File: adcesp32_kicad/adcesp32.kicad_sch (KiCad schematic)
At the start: 16 parts, among them IC1 PCM1862DBT, J1 AudioJack4, J2 USB_C_Receptacle_USB2.0_16P, J3 RCJ-2112, SW1 SW_Push, SW2 SW_Push, U1 ESP32-S3-WROOM-1, U2 AMS1117-3.3

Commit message: updated schematic
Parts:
- added C10, C11, C4, C5, C6, C7, C8, C9: C, symbol Device:C
- added D1, D2: LED, symbol Device:LED
- added J4, J5: Conn_01x05_Pin, symbol Connector:Conn_01x05_Pin
- added J6, J7: Conn_01x04_Pin, symbol Connector:Conn_01x04_Pin
- added L1: L_Small, symbol Device:L_Small
- added R6, R7: R, symbol Device:R
- IC1: footprint SOP50P640X120-30N -> KiCad:SOP50P640X120-30N
- J3: footprint RCJ2112 -> KiCad:RCJ2112
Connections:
- net +3V3: now also IC1.13 (DVDD), IC1.14 (IOVDD), C10.2, C11.2, C6.2, C7.2, J7.2 (Pin_2), L1.1, R7.2
- net BCK: now also J4.4 (Pin_4)
- net DOUT_ADC: now also J4.2 (Pin_2)
- net GND: now also IC1.12 (DGND), IC1.7 (AGND), C10.1, C11.1, C6.1, C7.1, C8.1, C9.1, D1.1 (K), D2.1 (K), J7.1 (Pin_1)
- net I2S_DOUT: now also J4.1 (Pin_1)
- net L1: now also C5.1; no longer IC1.3 (VINL1/VIN1P)
- net LRCK: now also J4.3 (Pin_3)
- net R1: now also C4.1; no longer IC1.4 (VINR1/VIN2P)
- net SCL: now also J7.3 (Pin_3)
- net SDA: now also J7.4 (Pin_4)
- net ESP_GPIO17: now reaches U1.10 (IO17)
- net ESP_GPIO17: now also J5.2 (Pin_2)
- net ESP_GPIO18: now reaches U1.11 (IO18)
- net ESP_GPIO18: now also J5.3 (Pin_3)
- net ESP_GPIO38: now reaches U1.31 (IO38)
- net ESP_GPIO38: now also J5.1 (Pin_1)
- net ESP_GPIO2: now reaches U1.38 (IO2)
- net ESP_GPIO2: now also J5.4 (Pin_4)
- net ESP_GPIO1: now reaches U1.39 (IO1)
- net ESP_GPIO1: now also J5.5 (Pin_5)
- net at U1.4 (IO4): now also R6.2
- net at IC1.11 (LDO): now also C9.2
- net SCKI: now reaches IC1.15 (SCKI)
- net SCKI: now also J4.5 (Pin_5)
- net ADC_GPIO3: now reaches IC1.19 (INT)
- net ADC_GPIO3: now also J6.4 (Pin_4)
- net ADC_GPIO2: now reaches IC1.20 (MD6)
- net ADC_GPIO2: now also J6.3 (Pin_3)
- net ADC_GPIO1: now reaches IC1.21 (MD5)
- net ADC_GPIO1: now also J6.2 (Pin_2)
- net ADC_GPIO0: now reaches IC1.22 (MD4)
- net ADC_GPIO0: now also J6.1 (Pin_1)
- net at IC1.6 (VREF): now also C8.2
- net AVDD: now reaches IC1.8 (AVDD)
- net AVDD: now also L1.2
- new net: C4.2, IC1.4 (VINR1/VIN2P)
- new net: C5.2, IC1.3 (VINL1/VIN1P)
- new net: D1.2 (A), R7.1
- new net: D2.2 (A), R6.1
- no-connect marks 3 -> 33
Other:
- moved on the sheet: C3, IC1, J1, J3, R2, R3, U1

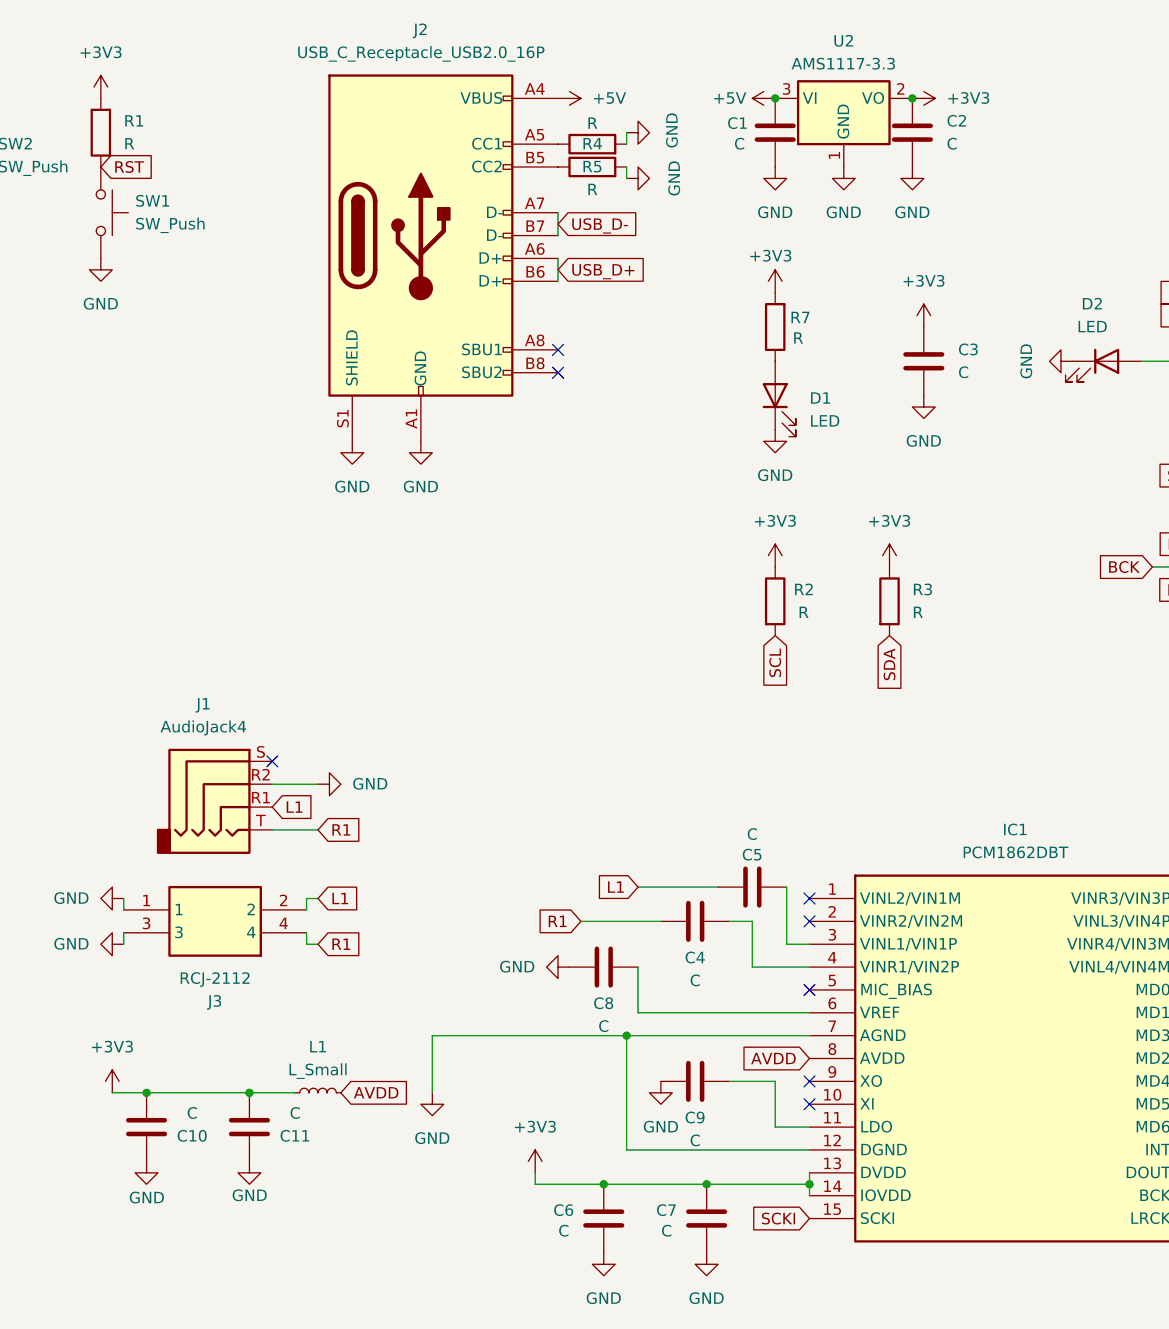
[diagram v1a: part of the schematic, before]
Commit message: added cap values
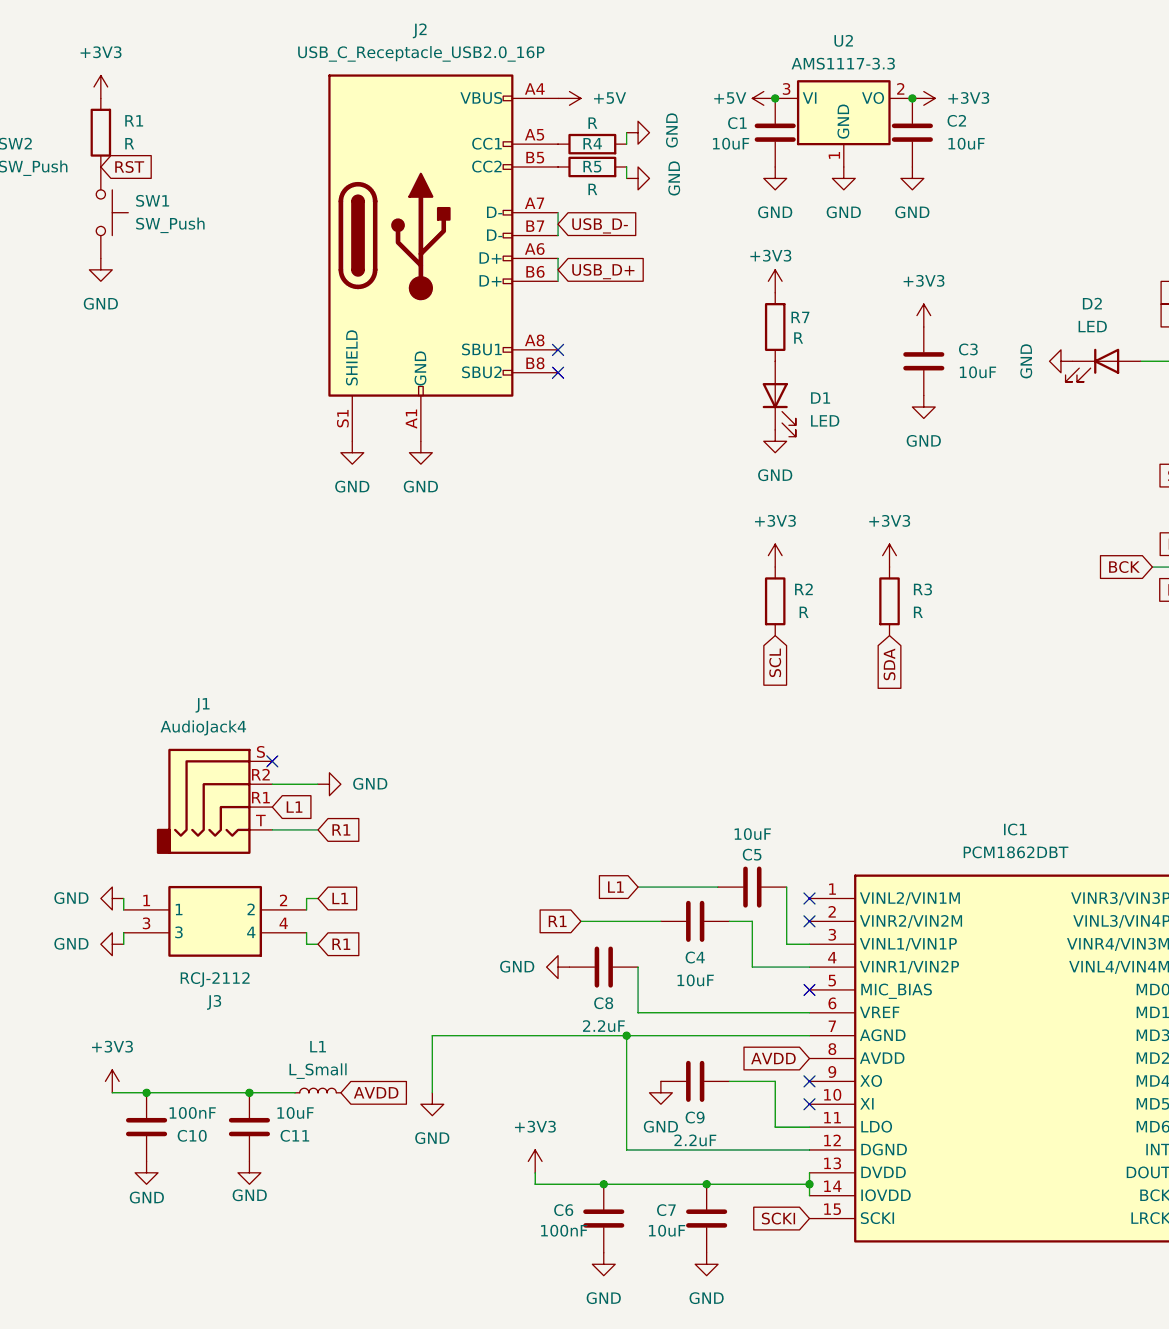
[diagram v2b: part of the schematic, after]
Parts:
- C1, C11, C2, C3, C4, C5, C7: value C -> 10uF; footprint (none) -> Capacitor_SMD:C_0402_1005Metric
- C10, C6: value C -> 100nF; footprint (none) -> Capacitor_SMD:C_0402_1005Metric
- C8, C9: value C -> 2.2uF; footprint (none) -> Capacitor_SMD:C_0402_1005Metric
- J4, J5: footprint (none) -> Connector_PinHeader_1.00mm:PinHeader_1x05_P1.00mm_Vertical
- J6, J7: footprint (none) -> Connector_PinHeader_1.00mm:PinHeader_1x04_P1.00mm_Vertical
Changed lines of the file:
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@@
 			)
 		)
-		(property "Footprint" ""
+		(property "Footprint" "Connector_PinHeader_1.00mm:PinHeader_1x04_P1.00mm_Vertical"
 			(at 248.92 146.05 0)
 			(effects
@@
 			)
 		)
-		(property "Value" "C"
+		(property "Value" "10uF"
 			(at 107.95 122.174 90)
 			(effects
@@
 			)
 		)
-		(property "Footprint" ""
+		(property "Footprint" "Capacitor_SMD:C_0402_1005Metric"
 			(at 111.76 114.6048 0)
 			(effects
@@
 			)
 		)
-		(property "Value" "C"
+		(property "Value" "10uF"
 			(at 135.89 29.2099 0)
 			(effects
@@
 			)
 		)
-		(property "Footprint" ""
+		(property "Footprint" "Capacitor_SMD:C_0402_1005Metric"
 			(at 133.0452 31.75 0)
 			(effects
@@
 			)
 		)
-		(property "Footprint" ""
+		(property "Footprint" "Connector_PinHeader_1.00mm:PinHeader_1x05_P1.00mm_Vertical"
 			(at 246.38 111.76 0)
 			(effects
@@
 			)
 		)
-		(property "Footprint" ""
+		(property "Footprint" "Connector_PinHeader_1.00mm:PinHeader_1x04_P1.00mm_Vertical"
 			(at 248.92 129.54 0)
 			(effects
@@
 			)
 		)
-		(property "Value" "C"
+		(property "Value" "10uF"
 			(at 114.3 105.918 90)
 			(effects
@@
 			)
 		)
-		(property "Footprint" ""
+		(property "Footprint" "Capacitor_SMD:C_0402_1005Metric"
 			(at 118.11 110.7948 0)
 			(effects
@@
 			)
 		)
-		(property "Value" "C"
+		(property "Value" "10uF"
 			(at 137.16 54.6099 0)
 			(effects
@@
 			)
 		)
-		(property "Footprint" ""
+		(property "Footprint" "Capacitor_SMD:C_0402_1005Metric"
 			(at 134.3152 57.15 0)
 			(effects
@@
 			)
 		)
-		(property "Value" "C"
+		(property "Value" "100nF"
 			(at 93.345 149.987 0)
 			(effects
@@
 			)
 		)
-		(property "Footprint" ""
+		(property "Footprint" "Capacitor_SMD:C_0402_1005Metric"
 			(at 96.8248 144.78 0)
 			(effects
@@
 			)
 		)
-		(property "Value" "C"
+		(property "Value" "10uF"
 			(at 104.775 149.987 0)
 			(effects
@@
 			)
 		)
-		(property "Footprint" ""
+		(property "Footprint" "Capacitor_SMD:C_0402_1005Metric"
 			(at 108.2548 144.78 0)
 			(effects
@@
 			)
 		)
-		(property "Value" "C"
+		(property "Value" "2.2uF"
 			(at 107.95 139.954 90)
 			(effects
@@
 			)
 		)
-		(property "Footprint" ""
+		(property "Footprint" "Capacitor_SMD:C_0402_1005Metric"
 			(at 111.76 132.3848 0)
 			(effects
@@
 			)
 		)
-		(property "Value" "C"
-			(at 112.268 29.21 0)
+		(property "Value" "10uF"
+			(at 109.728 29.21 0)
 			(effects
 				(font
@@
 			)
 		)
-		(property "Footprint" ""
+		(property "Footprint" "Capacitor_SMD:C_0402_1005Metric"
 			(at 117.8052 31.75 0)
 			(effects
@@
 			)
 		)
-		(property "Value" "C"
+		(property "Value" "2.2uF"
 			(at 97.79 127.254 90)
 			(effects
@@
 			)
 		)
-		(property "Footprint" ""
+		(property "Footprint" "Capacitor_SMD:C_0402_1005Metric"
 			(at 101.6 119.6848 0)
 			(effects
@@
 			)
 		)
-		(property "Footprint" ""
+		(property "Footprint" "Connector_PinHeader_1.00mm:PinHeader_1x05_P1.00mm_Vertical"
 			(at 246.38 92.71 0)
 			(effects
@@
 			)
 		)
-		(property "Value" "C"
+		(property "Value" "10uF"
 			(at 63.5 136.906 0)
 			(effects
@@
 			)
 		)
-		(property "Footprint" ""
+		(property "Footprint" "Capacitor_SMD:C_0402_1005Metric"
 			(at 57.4548 134.62 0)
 			(effects
@@
 			)
 		)
-		(property "Value" "C"
+		(property "Value" "100nF"
 			(at 52.07 136.906 0)
 			(effects
@@
 			)
 		)
-		(property "Footprint" ""
+		(property "Footprint" "Capacitor_SMD:C_0402_1005Metric"
 			(at 46.0248 134.62 0)
 			(effects

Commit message: completed pcb design
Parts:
- removed J1: AudioJack4, symbol Connector_Audio:AudioJack4
- removed SW1, SW2: SW_Push, symbol Switch:SW_Push
- added C12: 10uF, Capacitor_SMD:C_0402_1005Metric, symbol Device:C
- added J8: Conn_01x04_Pin, Connector_PinHeader_1.00mm:PinHeader_1x04_P1.00mm_Vertical, symbol Connector:Conn_01x04_Pin
- added J9: SJ-43514, SJ43514, symbol SJ-43514:SJ-43514
- added R8: 0.5Ohm, Resistor_SMD:R_0603_1608Metric, symbol Device:R
- added R9: 10kOhm, Resistor_SMD:R_0402_1005Metric, symbol Device:R
- added S1, S2, S3: TS-1187, KiCad:SW_TS-1187A-B-A-B, symbol TS-1187A-B-A-B:TS-1187A-B-A-B
- D1, D2: footprint (none) -> Resistor_SMD:R_0805_2012Metric
- J2: footprint (none) -> Connector_USB:USB_C_Receptacle_HRO_TYPE-C-31-M-12
- L1: value L_Small -> 10uH; footprint (none) -> Inductor_SMD:L_0805_2012Metric
- R1: value R -> 10kOhm; footprint (none) -> Resistor_SMD:R_0402_1005Metric
- R2, R3, R6, R7: value R -> 2.2kOhm; footprint (none) -> Resistor_SMD:R_0603_1608Metric
- R4, R5: value R -> 5.1kOhm; footprint (none) -> Resistor_SMD:R_0402_1005Metric
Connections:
- net +3V3: now also J8.4 (Pin_4), R8.2, R9.2; no longer C2.1
- net BOOT: now also S1.C, S1.D
- net GND: now also C12.1, J8.3 (Pin_3), J9.4 (RING_2), S1.A, S1.B, S2.A, S2.B, S3.A, S3.B
- net L1: now also J9.3 (RING_1)
- net R1: now also J9.2 (TIP)
- net RST: now also S2.C, S2.D
- net PHYS_INT: now reaches U1.28 (IO35)
- net PHYS_INT: now also C12.2, R9.1, S3.C, S3.D
- net RX: now reaches U1.36 (RXD0)
- net RX: now also J8.2 (Pin_2)
- net TX: now reaches U1.37 (TXD0)
- net TX: now also J8.1 (Pin_1)
- net ESP_GPIO4: now reaches R6.2, U1.4 (IO4)
- new net: C2.1, R8.1
- no-connect marks 33 -> 30
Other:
- moved on the sheet: C1, C10, C11, C2, C3, C4, C5, C6, C7, C8, C9, D1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

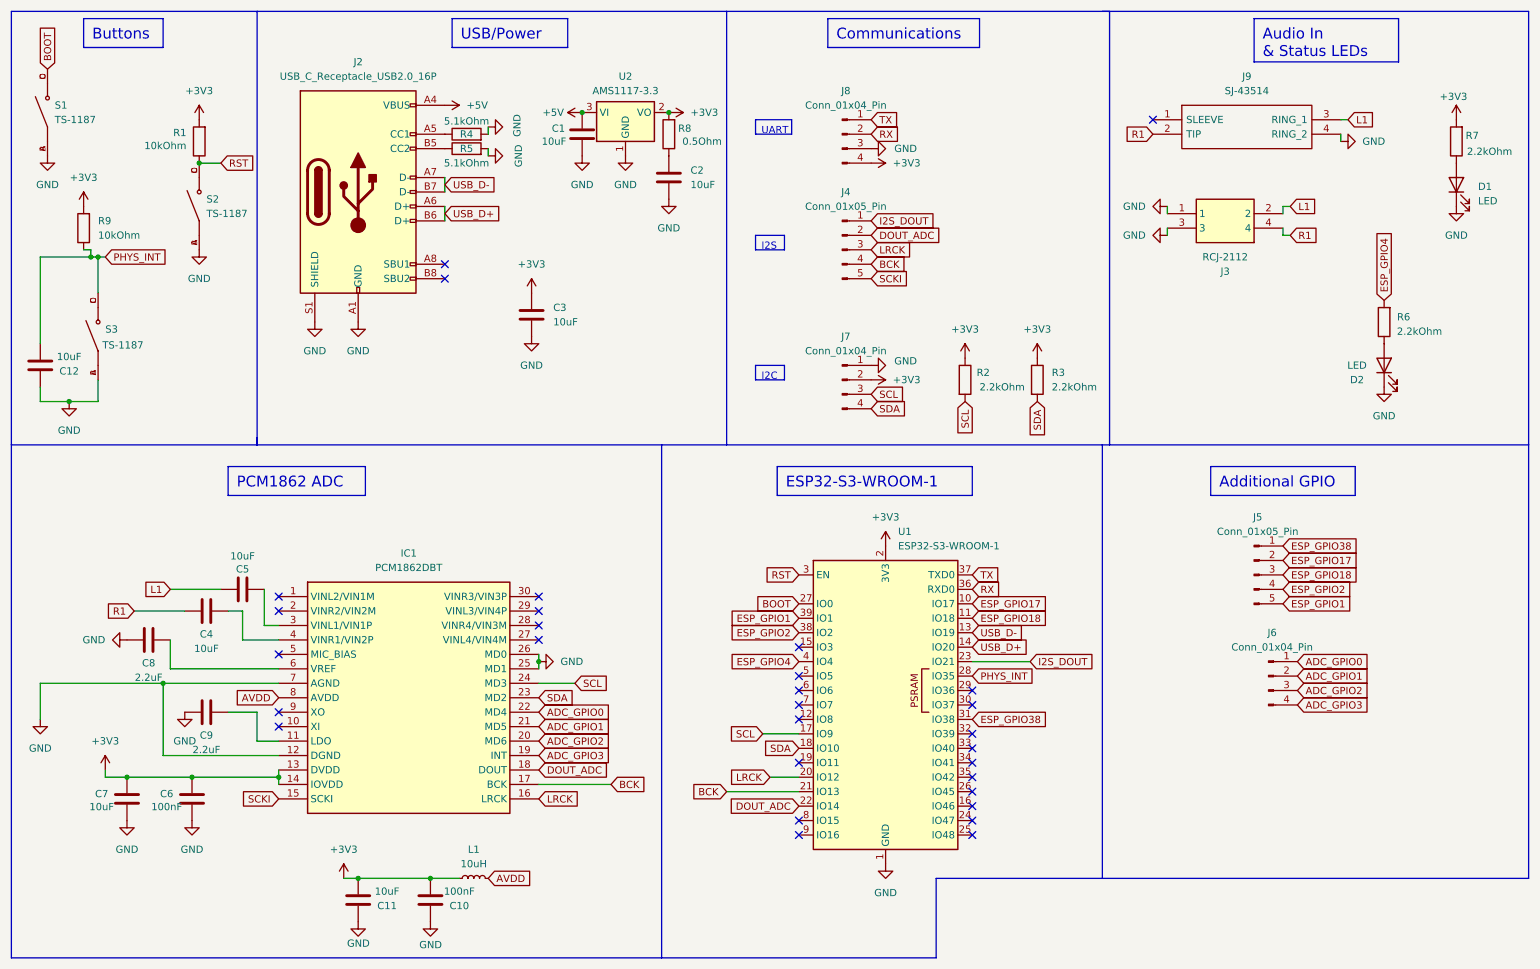
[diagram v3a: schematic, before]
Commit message: completed 52x52 pcb design
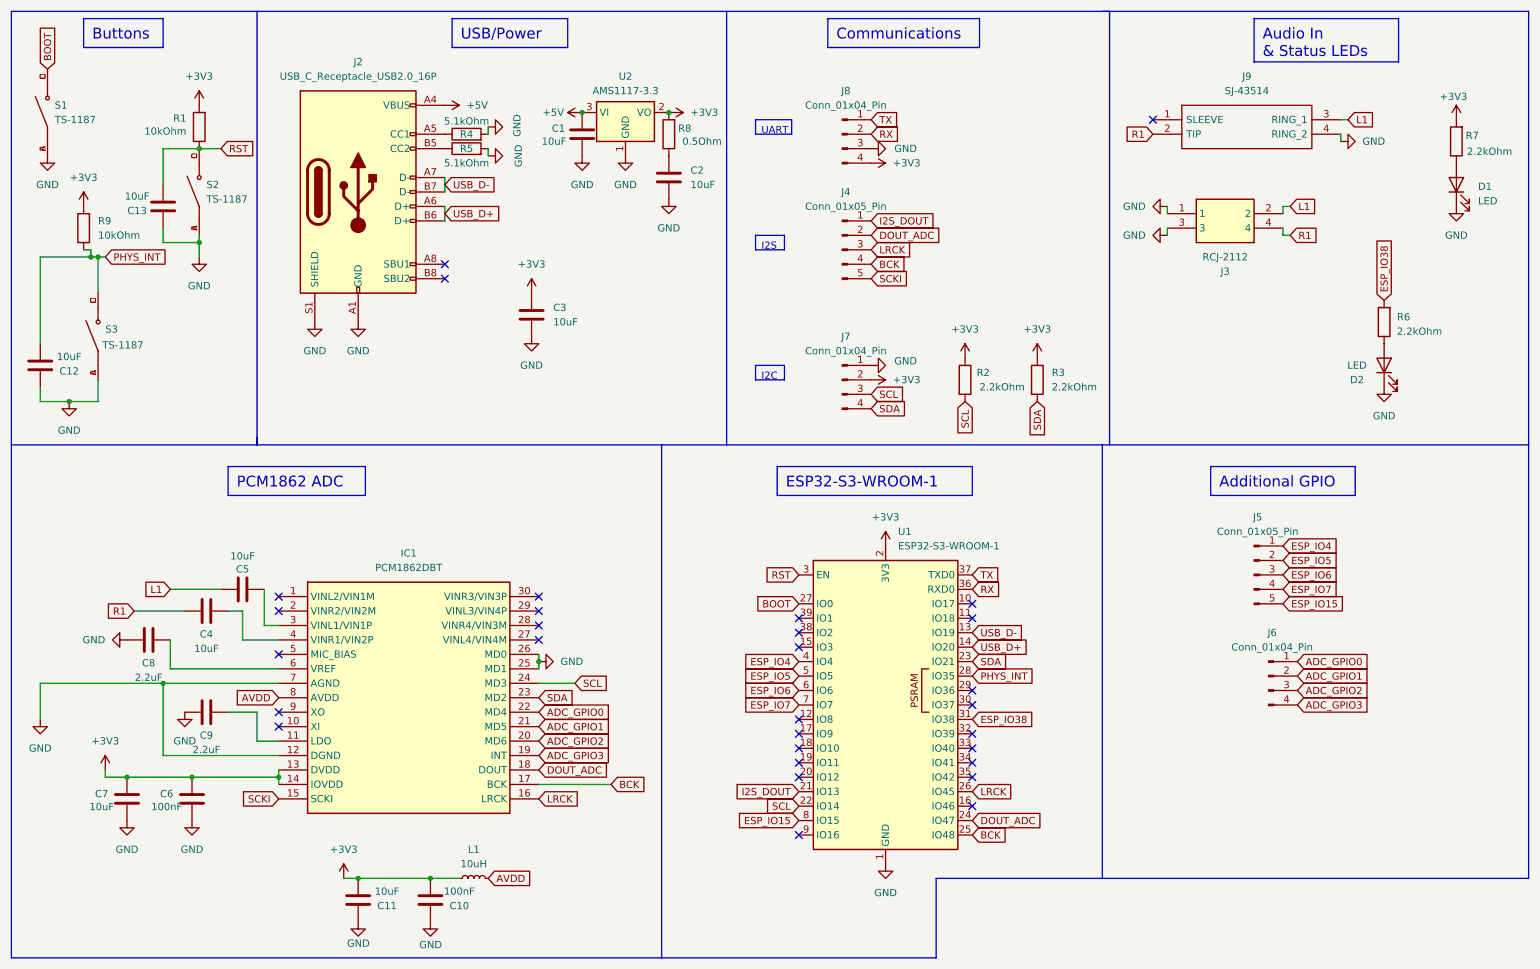
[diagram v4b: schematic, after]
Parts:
- added C13: 10uF, Capacitor_SMD:C_0402_1005Metric, symbol Device:C
- J4, J5: footprint Connector_PinHeader_1.00mm:PinHeader_1x05_P1.00mm_Vertical -> Connector_PinHeader_2.54mm:PinHeader_1x05_P2.54mm_Vertical
- J6, J7, J8: footprint Connector_PinHeader_1.00mm:PinHeader_1x04_P1.00mm_Vertical -> Connector_PinHeader_2.54mm:PinHeader_1x04_P2.54mm_Vertical
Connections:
- net BCK: now also U1.25 (IO48); no longer U1.21 (IO13)
- net DOUT_ADC: now also U1.24 (IO47); no longer U1.22 (IO14)
- net GND: now also C13.1
- net I2S_DOUT: now also U1.21 (IO13); no longer U1.23 (IO21)
- net LRCK: now also U1.26 (IO45); no longer U1.20 (IO12)
- net RST: now also C13.2
- net SCL: now also U1.22 (IO14); no longer U1.17 (IO9)
- net SDA: now also U1.23 (IO21); no longer U1.18 (IO10)
- net ESP_IO5: now reaches U1.5 (IO5)
- net ESP_IO5: now also J5.2 (Pin_2)
- net ESP_IO6: now reaches U1.6 (IO6)
- net ESP_IO6: now also J5.3 (Pin_3)
- net ESP_IO7: now reaches U1.7 (IO7)
- net ESP_IO7: now also J5.4 (Pin_4)
- net ESP_IO15: now reaches U1.8 (IO15)
- net ESP_IO15: now also J5.5 (Pin_5)
- net ESP_GPIO1: no longer names the net of U1.39 (IO1)
- net ESP_GPIO1: no longer J5.5 (Pin_5)
- net ESP_GPIO17: no longer names the net of U1.10 (IO17)
- net ESP_GPIO17: no longer J5.2 (Pin_2)
- net ESP_GPIO18: no longer names the net of U1.11 (IO18)
- net ESP_GPIO18: no longer J5.3 (Pin_3)
- net ESP_GPIO2: no longer names the net of U1.38 (IO2)
- net ESP_GPIO2: no longer J5.4 (Pin_4)
- net ESP_GPIO38 renamed ESP_IO38
- net ESP_IO38: now also R6.2; no longer J5.1 (Pin_1)
- net ESP_GPIO4 renamed ESP_IO4
- net ESP_IO4: now also J5.1 (Pin_1); no longer R6.2
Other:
- moved on the sheet: R1, S2
